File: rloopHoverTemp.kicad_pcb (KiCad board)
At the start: 2 copper layers, 40 x 50 mm, 23 parts, among them P1 CONN_01X01, P2 CONN_01X01, P3 CONN_01X01, P4 CONN_01X01, U1 P82B715TD, U2 MLX90614, U3 Regulator, U4 Regulator, X1 RJ45-SHIELDED, X2 RJ45-SHIELDED

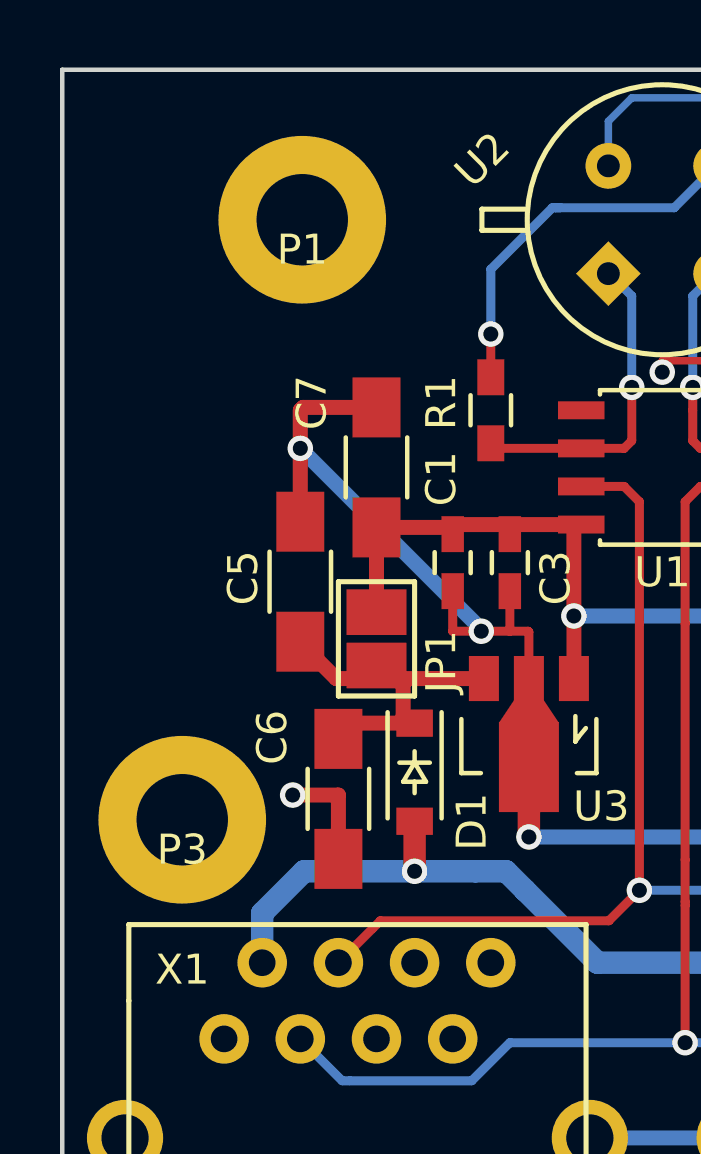
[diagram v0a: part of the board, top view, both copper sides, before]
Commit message: removed grounds from screw holes, added a silk label
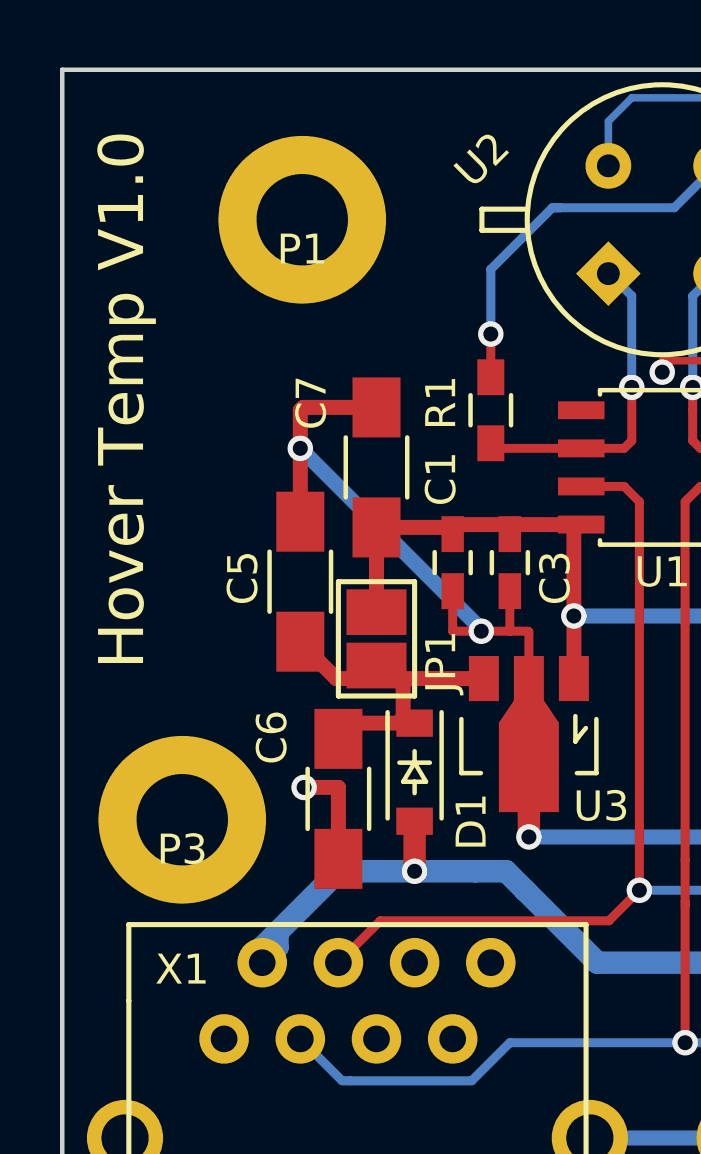
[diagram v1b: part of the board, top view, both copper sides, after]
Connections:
- P1 pad 1: GND -> Net-(P1-Pad1)
- P2 pad 1: GND -> Net-(P2-Pad1)
- P3 pad 1: GND -> Net-(P3-Pad1)
- P4 pad 1: GND -> Net-(P4-Pad1)
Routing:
- net +24V: track 25.6 -> 26.2 mm
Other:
- net class HOLES added: clearance 0.8, trace_width 0.25, via_dia 0.85, via_drill 0.5
- board text added: "Bottom"
- board text added: "Hover Temp V1.0"
- board text added: "Top"
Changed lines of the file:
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@@
 (kicad_pcb (version 4) (host pcbnew 4.0.2-stable)
   (general
-    (links 60)
+    (links 56)
     (no_connects 4)
-    (area 0 0 0 0)
+    (area -0.735001 -0.735001 101.785715 114.200001)
     (thickness 1.6)
-    (drawings 22)
-    (tracks 192)
+    (drawings 26)
+    (tracks 196)
     (zones 0)
     (modules 23)
-    (nets 14)
+    (nets 17)
   )
   (page A4)
@@
   )
   (setup
-    (last_trace_width 0.5)
+    (last_trace_width 0.25)
     (user_trace_width 0.3)
     (user_trace_width 0.4)
@@
   (net 10 SDA)
   (net 11 SCL)
-  (net 12 "Net-(X1-PadSHLD)")
-  (net 13 /CABLE-SHIELD)
+  (net 12 /CABLE-SHIELD)
+  (net 13 "Net-(P1-Pad1)")
+  (net 14 "Net-(P2-Pad1)")
+  (net 15 "Net-(P3-Pad1)")
+  (net 16 "Net-(P4-Pad1)")
   (net_class Default "This is the default net class."
     (clearance 0.25)
@@
     (add_net SDA)
   )
+  (net_class HOLES ""
+    (clearance 0.8)
+    (trace_width 0.25)
+    (via_dia 0.85)
+    (via_drill 0.5)
+    (uvia_dia 0.3)
+    (uvia_drill 0.1)
+    (add_net "Net-(P1-Pad1)")
+    (add_net "Net-(P2-Pad1)")
+    (add_net "Net-(P3-Pad1)")
+    (add_net "Net-(P4-Pad1)")
+  )
   (module Capacitors_SMD:C_0603_HandSoldering (layer F.Cu)
     (at 58.42 74.93 90)
@@
     )
     (pad 1 thru_hole circle (at 0 0) (size 5.588 5.588) (drill 3.048) (layers *.Cu *.Mask F.SilkS)
-      (net 1 GND))
+      (net 13 "Net-(P1-Pad1)"))
   )
   (module -footprints:SCREWPAD-4-40 (layer F.Cu)
@@
     )
     (pad 1 thru_hole circle (at 0 0) (size 5.588 5.588) (drill 3.048) (layers *.Cu *.Mask F.SilkS)
-      (net 1 GND))
+      (net 14 "Net-(P2-Pad1)"))
   )
   (module -footprints:SCREWPAD-4-40 (layer F.Cu)
@@
     )
     (pad 1 thru_hole circle (at 0 0) (size 5.588 5.588) (drill 3.048) (layers *.Cu *.Mask F.SilkS)
-      (net 1 GND))
+      (net 15 "Net-(P3-Pad1)"))
   )
   (module -footprints:SCREWPAD-4-40 (layer F.Cu)
@@
     )
     (pad 1 thru_hole circle (at 0 0) (size 5.588 5.588) (drill 3.048) (layers *.Cu *.Mask F.SilkS)
-      (net 1 GND))
+      (net 16 "Net-(P4-Pad1)"))
   )
   (module -footprints:RJ45-TE-5558342-1 (layer F.Cu)
@@
     (pad "" np_thru_hole circle (at 5.715 7.62) (size 3.2512 3.2512) (drill 3.2512) (layers *.Cu *.Mask F.SilkS))
     (pad SHLD thru_hole circle (at -7.747 4.572) (size 2.54 2.54) (drill 1.5748) (layers *.Cu *.Mask)
-      (net 13 /CABLE-SHIELD))
+      (net 12 /CABLE-SHIELD))
     (pad SHLD thru_hole circle (at 7.747 4.572) (size 2.54 2.54) (drill 1.5748) (layers *.Cu *.Mask)
-      (net 13 /CABLE-SHIELD))
+      (net 12 /CABLE-SHIELD))
   )
   (module -footprints:RJ45-TE-5558342-1 (layer F.Cu)
@@
     (pad "" np_thru_hole circle (at 5.715 7.62) (size 3.2512 3.2512) (drill 3.2512) (layers *.Cu *.Mask F.SilkS))
     (pad SHLD thru_hole circle (at -7.747 4.572) (size 2.54 2.54) (drill 1.5748) (layers *.Cu *.Mask)
-      (net 13 /CABLE-SHIELD))
+      (net 12 /CABLE-SHIELD))
     (pad SHLD thru_hole circle (at 7.747 4.572) (size 2.54 2.54) (drill 1.5748) (layers *.Cu *.Mask)
-      (net 13 /CABLE-SHIELD))
+      (net 12 /CABLE-SHIELD))
+  )
+  (gr_text Bottom (at 78.5 68.5) (layer B.Mask)
+    (effects (font (size 1.5 1.5) (thickness 0.3)) (justify mirror))
+  )
+  (gr_text Top (at 80.5 68.5) (layer F.Mask)
+    (effects (font (size 1.5 1.5) (thickness 0.3)))
+  )
+  (gr_text "Hover Temp V1.0" (at 45.5 69.5 90) (layer B.SilkS)
+    (effects (font (size 1.5 1.5) (thickness 0.3)) (justify mirror))
+  )
+  (gr_text "Hover Temp V1.0" (at 45.5 69.5 90) (layer F.SilkS)
+    (effects (font (size 1.5 1.5) (thickness 0.3)))
   )
   (gr_line (start 43.5 108.5) (end 43.5 58.5) (angle 90) (layer Edge.Cuts) (width 0.15))
@@
   (via (at 63.5 68.58) (size 0.85) (drill 0.5) (layers F.Cu B.Cu) (net 1))
   (segment (start 63.5 68.199) (end 63.5 68.58) (width 0.25) (layer F.Cu) (net 1))
-  (segment (start 52.705 84.55) (end 52.705 82.677) (width 0.5) (layer F.Cu) (net 1))
-  (via (at 51.181 82.677) (size 0.85) (drill 0.5) (layers F.Cu B.Cu) (net 1))
-  (segment (start 52.705 82.677) (end 51.181 82.677) (width 0.5) (layer F.Cu) (net 1))
+  (segment (start 52.705 84.55) (end 52.705 82.423) (width 0.5) (layer F.Cu) (net 1))
+  (via (at 51.562 82.423) (size 0.85) (drill 0.5) (layers F.Cu B.Cu) (net 1))
+  (segment (start 52.705 82.423) (end 51.562 82.423) (width 0.5) (layer F.Cu) (net 1))
   (segment (start 66.675 82.804) (end 66.675 82.645) (width 0.5) (layer F.Cu) (net 1))
   (segment (start 52.705 84.582) (end 52.705 84.55) (width 0.4) (layer F.Cu) (net 1))
@@
   (segment (start 52.63134 78.79334) (end 51.435 77.597) (width 0.5) (layer F.Cu) (net 4))
   (segment (start 51.435 77.597) (end 51.435 77.565) (width 0.5) (layer F.Cu) (net 4))
+  (segment (start 50.673 87.249) (end 50.673 87.757) (width 0.75) (layer B.Cu) (net 5))
+  (segment (start 50.673 87.757) (end 50.165 88.265) (width 0.75) (layer B.Cu) (net 5))
+  (segment (start 55.245 85.217) (end 52.705 85.217) (width 0.75) (layer B.Cu) (net 5))
+  (segment (start 52.705 85.217) (end 50.673 87.249) (width 0.75) (layer B.Cu) (net 5))
+  (segment (start 50.673 87.249) (end 50.165 87.757) (width 0.75) (layer B.Cu) (net 5))
+  (segment (start 50.165 87.757) (end 50.165 88.265) (width 0.75) (layer B.Cu) (net 5))
   (segment (start 58.928 85.852) (end 58.293 85.217) (width 0.75) (layer B.Cu) (net 5))
   (segment (start 61.341 88.265) (end 58.928 85.852) (width 0.75) (layer B.Cu) (net 5))
+  (segment (start 55.245 85.217) (end 55.245 85.217) (width 0.75) (layer B.Cu) (net 5))
   (segment (start 55.245 85.217) (end 57.277 85.217) (width 0.75) (layer B.Cu) (net 5))
   (segment (start 61.341 88.265) (end 70.485 88.265) (width 0.75) (layer B.Cu) (net 5))
   (segment (start 58.293 85.217) (end 57.277 85.217) (width 0.75) (layer B.Cu) (net 5))
-  (segment (start 55.245 85.217) (end 51.562 85.217) (width 0.75) (layer B.Cu) (net 5))
-  (segment (start 50.165 86.614) (end 50.165 88.265) (width 0.75) (layer B.Cu) (net 5))
-  (segment (start 51.562 85.217) (end 50.165 86.614) (width 0.75) (layer B.Cu) (net 5))
   (segment (start 55.245 85.217) (end 55.245 83.55) (width 0.75) (layer F.Cu) (net 5))
   (via (at 55.245 85.217) (size 0.85) (drill 0.5) (layers F.Cu B.Cu) (net 5))
@@
   (segment (start 62.738 85.852) (end 70.612 85.852) (width 0.3) (layer B.Cu) (net 11))
   (segment (start 72.898 88.138) (end 73.025 88.265) (width 0.3) (layer B.Cu) (net 11))
-  (segment (start 61.087 94.107) (end 65.913 94.107) (width 0.5) (layer B.Cu) (net 13))
+  (segment (start 61.087 94.107) (end 65.913 94.107) (width 0.5) (layer B.Cu) (net 12))
   (zone (net 1) (net_name GND) (layer F.Cu) (hatch edge 0.508)
     (connect_pads (clearance 0.254))

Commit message: missed two capacitor values
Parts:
- C1: value C -> 100n
- C3: value C -> 1u
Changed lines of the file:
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@@
     (links 56)
     (no_connects 4)
-    (area -0.735001 -0.735001 101.785715 114.200001)
+    (area 43.424999 58.424999 83.575001 108.575001)
     (thickness 1.6)
     (drawings 26)
@@
       (effects (font (size 1 1) (thickness 0.15)))
     )
-    (fp_text value C (at 0 1.9 90) (layer F.Fab)
+    (fp_text value 100n (at 0 1.9 90) (layer F.Fab)
       (effects (font (size 1 1) (thickness 0.15)))
     )
@@
       (effects (font (size 1 1) (thickness 0.15)))
     )
-    (fp_text value C (at 0 1.9 270) (layer F.Fab)
-      (effects (font (size 1 1) (thickness 0.15)))
-    )
+    (fp_text value 1u (at 0 1.9 270) (layer F.Fab)
+      (effects (font (size 1 1) (thickness 0.15)))
+    )
